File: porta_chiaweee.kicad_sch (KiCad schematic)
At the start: 3 parts, among them SW1 SW_Push

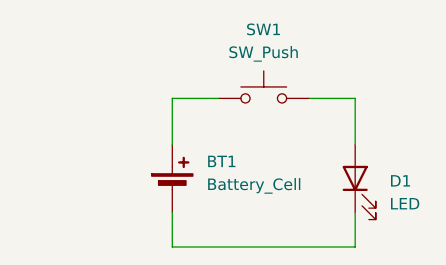
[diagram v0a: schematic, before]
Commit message: forma pcb e buco
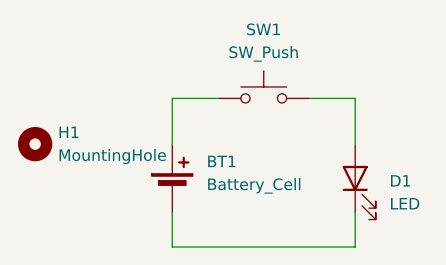
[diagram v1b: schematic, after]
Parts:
- added H1: MountingHole, MountingHole:MountingHole_5.3mm_M5_DIN965_Pad_TopBottom, symbol Mechanical:MountingHole
- BT1: footprint Battery:BatteryHolder_Keystone_1060_1x2032 -> Battery:BatteryHolder_Keystone_1058_1x2032
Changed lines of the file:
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@@
 			)
 		)
-		(property "Footprint" "Battery:BatteryHolder_Keystone_1060_1x2032"
+		(property "Footprint" "Battery:BatteryHolder_Keystone_1058_1x2032"
 			(at 104.14 58.166 90)
 			(effects
@@
 					(unit 1)
 				)
+			)
+		)
+	)
+	(symbol
+		(lib_id "Mechanical:MountingHole")
+		(at 88.9 54.61 0)
+		(unit 1)
+		(exclude_from_sim no)
+		(in_bom no)
+		(on_board yes)
+		(dnp no)
+		(fields_autoplaced yes)
+		(property "Reference" "H1"
+			(at 91.44 53.3399 0)
+			(effects
+				(font
+					(size 1.27 1.27)
+				)
+				(justify left)
+			)
+		)
+		(property "Value" "MountingHole"
+			(at 91.44 55.8799 0)
+			(effects
+				(font
+					(size 1.27 1.27)
+				)
+				(justify left)
+			)
+		)
+		(property "Footprint" "MountingHole:MountingHole_5.3mm_M5_DIN965_Pad_TopBottom"
+			(at 88.9 54.61 0)
+			(effects
+				(font
+					(size 1.27 1.27)
+				)
+				(hide yes)
+			)
+		)
+		(property "Datasheet" "~"
+			(at 88.9 54.61 0)
+			(effects
+				(font
+					(size 1.27 1.27)
+				)
+				(hide yes)
+			)
+		)
+		(property "Description" "Mounting Hole without connection"
+			(at 88.9 54.61 0)
+			(effects
+				(font
+					(size 1.27 1.27)
+				)
+				(hide yes)
+			)
+		)
+		(instances
+			(project ""
+				(path "/e2ee8c30-187f-4232-9917-a4730bf5bef2"
+					(reference "H1")
+					(unit 1)
+				)

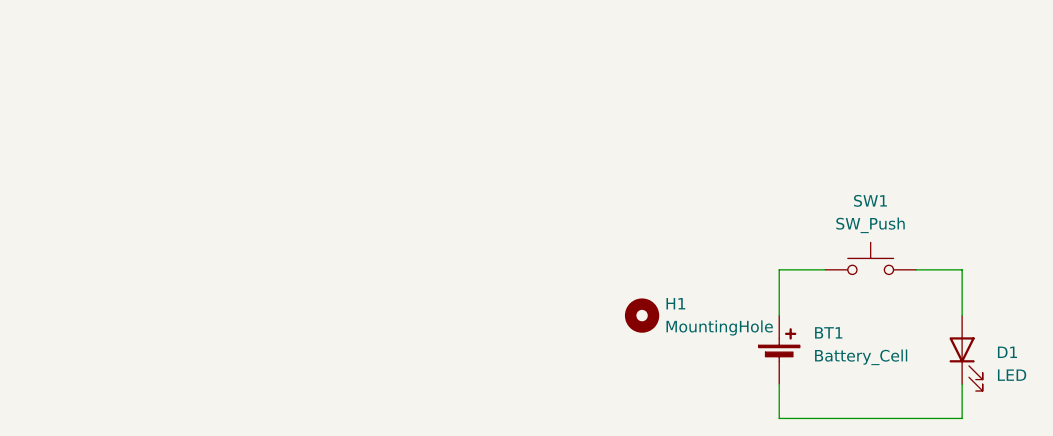
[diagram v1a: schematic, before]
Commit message: aggiunte librerie nuove e modelli 3D
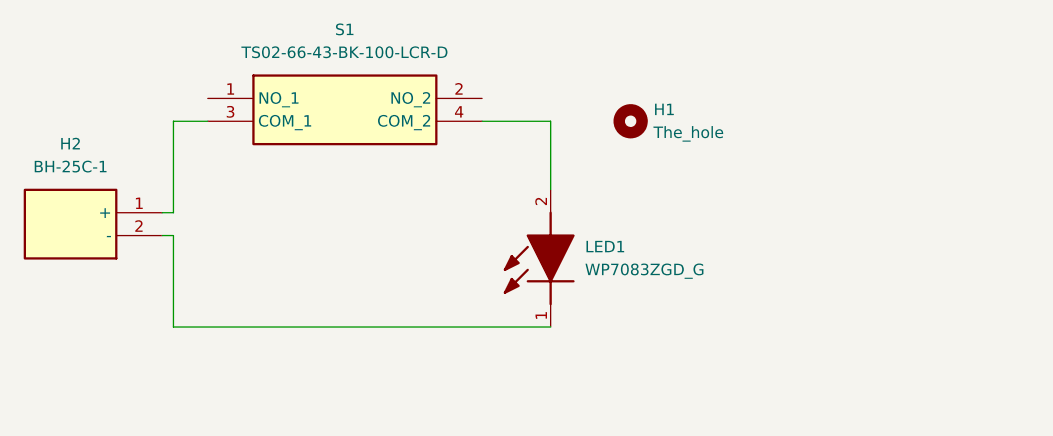
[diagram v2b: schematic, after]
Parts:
- removed BT1: Battery_Cell, Battery:BatteryHolder_Keystone_1058_1x2032, symbol Device:Battery_Cell
- removed D1: LED, LED_THT:LED_Rectangular_W3.9mm_H1.8mm, symbol Device:LED
- removed SW1: SW_Push, Button_Switch_THT:SW_PUSH_6mm_H13mm, symbol Switch:SW_Push
- added H2: BH-25C-1, BH25C1, symbol BH-25C-1:BH-25C-1
- added LED1: WP7083ZGD_G, L53ND, symbol WP7083ZGD_G:WP7083ZGD_G
- added S1: TS02-66-43-BK-100-LCR-D, TS026643BK100LCRD, symbol TS02-66-43-BK-100-LCR-D:TS02-66-43-BK-100-LCR-D
- H1: value MountingHole -> The_hole
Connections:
- new net: H2.1 (+), S1.3 (COM_1)
- new net: H2.2 (-), LED1.1 (K)
- new net: LED1.2 (A), S1.4 (COM_2)
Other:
- moved on the sheet: H1
